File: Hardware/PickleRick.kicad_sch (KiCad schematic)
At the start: 63 parts, among them J1 RBUS, J12 Conn_01x03_Male, J14 Conn_01x07_Socket, J2 Conn_01x02_Male, J3 ST1W008S4TR2000, J4 Conn_01x03_Pin, Q1 PMV20ENR, U1 ESP32-S3, U2 DPS368, Y1 R940000171

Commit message: update
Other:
- moved on the sheet: D19
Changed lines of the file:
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@@
 	(wire
 		(pts
-			(xy 121.92 181.61) (xy 138.43 181.61)
+			(xy 121.92 182.88) (xy 133.35 182.88)
 		)
 		(stroke
@@
 	(wire
 		(pts
-			(xy 121.92 189.23) (xy 121.92 181.61)
+			(xy 121.92 190.5) (xy 121.92 182.88)
 		)
 		(stroke
@@
 	)
 	(label "JTAG_MTDI"
-		(at 168.91 184.15 0)
+		(at 163.83 185.42 0)
 		(fields_autoplaced yes)
 		(effects
@@
 	)
 	(label "JTAG_MTDO"
-		(at 138.43 186.69 180)
+		(at 133.35 187.96 180)
 		(fields_autoplaced yes)
 		(effects
@@
 	)
 	(label "JTAG_MTMS"
-		(at 138.43 184.15 180)
+		(at 133.35 185.42 180)
 		(fields_autoplaced yes)
 		(effects
@@
 		(lib_name "GND_1")
 		(lib_id "power:GND")
-		(at 121.92 189.23 0)
+		(at 121.92 190.5 0)
 		(unit 1)
 		(exclude_from_sim no)
@@
 		(fields_autoplaced yes)
 		(property "Reference" "#PWR024"
-			(at 121.92 195.58 0)
+			(at 121.92 196.85 0)
 			(effects
 				(font
@@
 		)
 		(property "Value" "GND"
-			(at 121.92 194.31 0)
+			(at 121.92 195.58 0)
 			(effects
 				(font
@@
 		)
 		(property "Footprint" ""
-			(at 121.92 189.23 0)
+			(at 121.92 190.5 0)
 			(effects
 				(font
@@
 		)
 		(property "Datasheet" ""
-			(at 121.92 189.23 0)
+			(at 121.92 190.5 0)
 			(effects
 				(font
@@
 		)
 		(property "Description" "Power symbol creates a global label with name \"GND\" , ground"
-			(at 121.92 189.23 0)
+			(at 121.92 190.5 0)
 			(effects
 				(font
@@
 	(symbol
 		(lib_id "iclr-hw:RCLAMP3346PQTNT")
-		(at 138.43 179.07 0)
+		(at 133.35 180.34 0)
 		(unit 1)
 		(exclude_from_sim no)
@@
 		(fields_autoplaced yes)
 		(property "Reference" "D19"
-			(at 153.67 171.45 0)
+			(at 148.59 172.72 0)
 			(effects
 				(font
@@
 		)
 		(property "Value" "RCLAMP3346PQTNT"
-			(at 153.67 173.99 0)
+			(at 148.59 175.26 0)
 			(effects
 				(font
@@
 		)
 		(property "Footprint" "RCLAMP3346PQTNT"
-			(at 165.1 273.99 0)
+			(at 160.02 275.26 0)
 			(effects
 				(font
@@
 		)
 		(property "Datasheet" ""
-			(at 165.1 373.99 0)
+			(at 160.02 375.26 0)
 			(effects
 				(font
@@
 		)
 		(property "Description" "ESD Suppressors / TVS Diodes 6Line ESD protection automotive grade"
-			(at 138.43 179.07 0)
+			(at 133.35 180.34 0)
 			(effects
 				(font
@@
 		)
 		(property "Height" "0.53"
-			(at 165.1 573.99 0)
+			(at 160.02 575.26 0)
 			(effects
 				(font
@@
 		)
 		(property "Mouser Part Number" "947-RCLAMP3346PQTNT"
-			(at 165.1 673.99 0)
+			(at 160.02 675.26 0)
 			(effects
 				(font
@@
 		)
 		(property "Mouser Price/Stock" "https://www.mouser.co.uk/ProductDetail/Semtech/RCLAMP3346PQTNT?qs=gTYE2QTfZfTlZML4DB76Nw%3D%3D"
-			(at 165.1 773.99 0)
+			(at 160.02 775.26 0)
 			(effects
 				(font
@@
 		)
 		(property "Manufacturer_Name" "SEMTECH"
-			(at 165.1 873.99 0)
+			(at 160.02 875.26 0)
 			(effects
 				(font
@@
 		)
 		(property "Manufacturer_Part_Number" "RCLAMP3346PQTNT"
-			(at 165.1 973.99 0)
+			(at 160.02 975.26 0)
 			(effects
 				(font

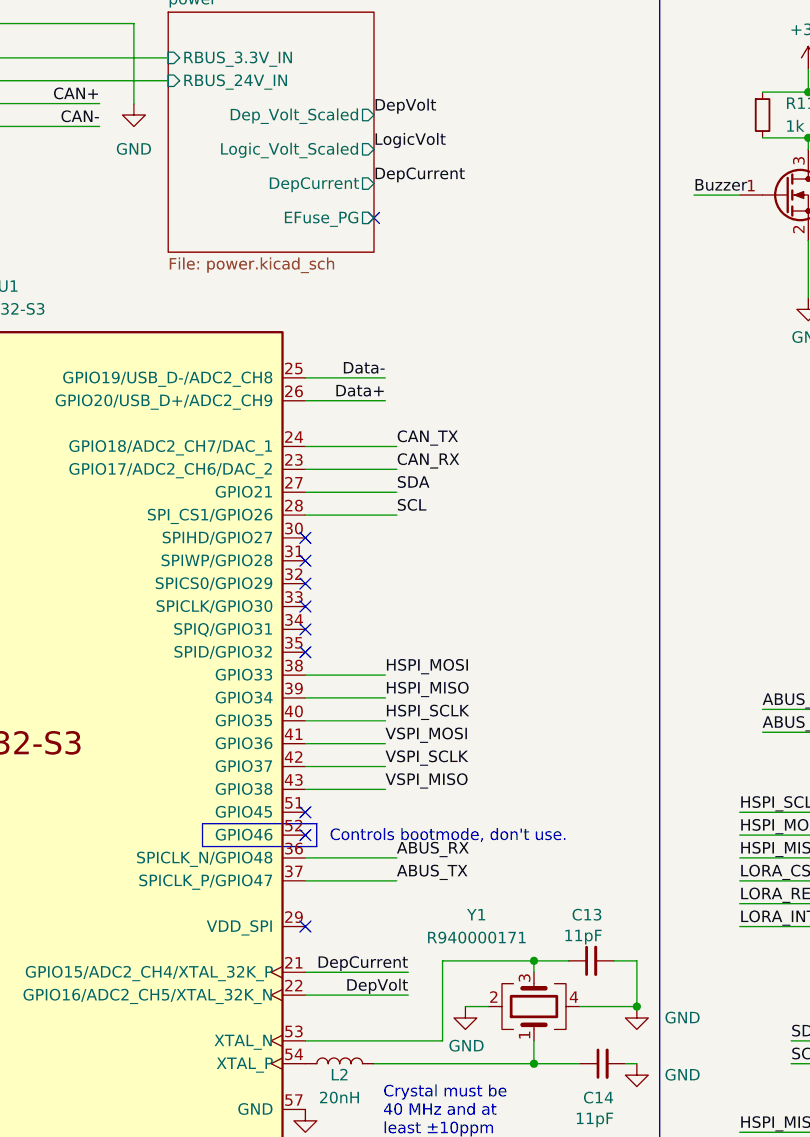
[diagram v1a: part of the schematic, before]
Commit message: replaced efuse with ina219
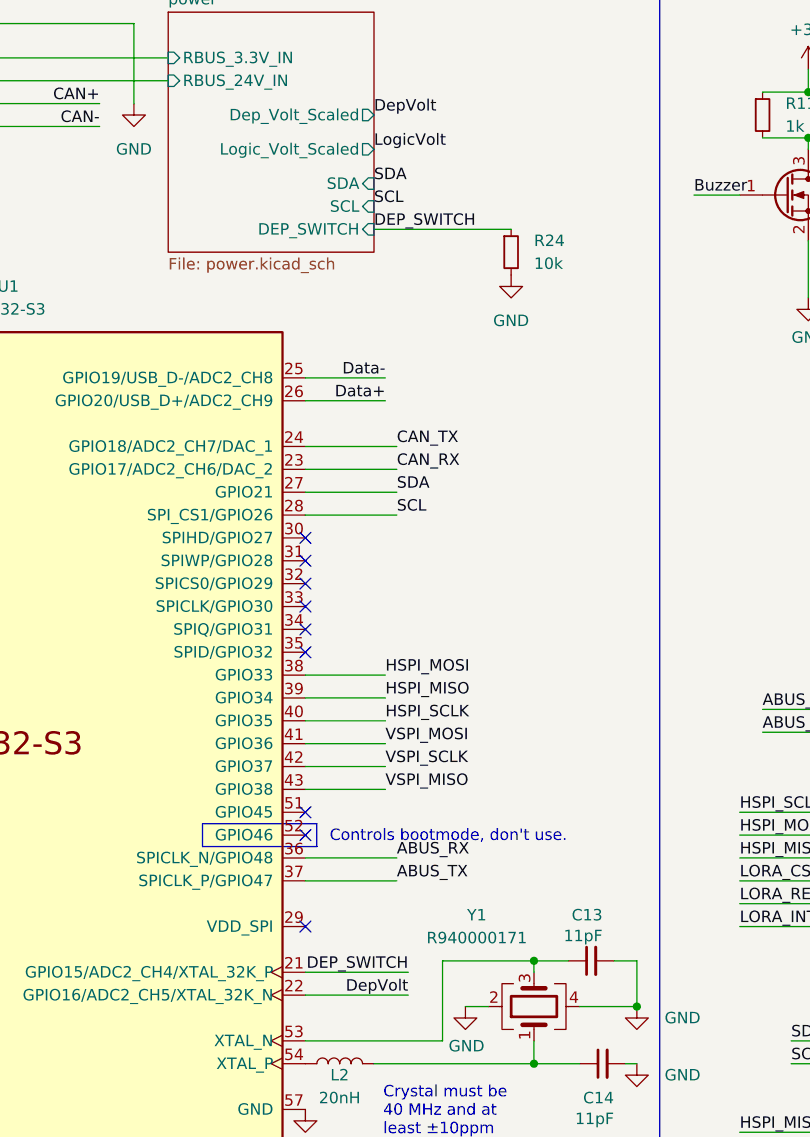
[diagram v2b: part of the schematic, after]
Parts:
- added R24: 10k, Resistor_SMD:R_0402_1005Metric, symbol Device:R_Small
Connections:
- net GND: now also R24.2
- net DepCurrent renamed DEP_SWITCH
- net DEP_SWITCH: now also R24.1
- no-connect marks 14 -> 13
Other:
- sheet power ports: added DEP_SWITCH, SCL, SDA; removed DepCurrent, EFuse_PG
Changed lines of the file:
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@@
 	)
 	(no_connect
-		(at 142.24 44.45)
-	)
-	(no_connect
 		(at 134.62 82.55)
 	)
@@
 	(wire
 		(pts
+			(xy 142.24 45.72) (xy 157.48 45.72)
+		)
+		(stroke
+			(width 0)
+			(type default)
+		)
+	)
+	(wire
+		(pts
 			(xy 226.06 123.19) (xy 234.95 123.19)
 		)
@@
 		)
 	)
+	(label "SDA"
+		(at 142.24 40.64 0)
+		(fields_autoplaced yes)
+		(effects
+			(font
+				(size 1.27 1.27)
+			)
+			(justify left bottom)
+		)
+	)
 	(label "LORA_RESET"
 		(at 60.96 92.71 180)
@@
 		)
 	)
-	(label "JTAG_MTMS"
-		(at 39.37 125.73 0)
+	(label "DEP_SWITCH"
+		(at 142.24 45.72 0)
 		(fields_autoplaced yes)
 		(effects
@@
 		)
 	)
-	(label "CAN-"
-		(at 114.3 187.96 0)
+	(label "JTAG_MTMS"
+		(at 39.37 125.73 0)
 		(fields_autoplaced yes)
 		(effects
@@
 		)
 	)
-	(label "DepCurrent"
-		(at 142.24 40.64 0)
+	(label "CAN-"
+		(at 114.3 187.96 0)
 		(fields_autoplaced yes)
 		(effects
@@
 		)
 	)
+	(label "SCL"
+		(at 142.24 43.18 0)
+		(fields_autoplaced yes)
+		(effects
+			(font
+				(size 1.27 1.27)
+			)
+			(justify left bottom)
+		)
+	)
 	(label "IMU2_CS"
 		(at 60.96 97.79 180)
@@
 		)
 	)
-	(label "DepCurrent"
+	(label "DEP_SWITCH"
 		(at 146.05 128.27 180)
 		(fields_autoplaced yes)
@@
 	)
 	(symbol
+		(lib_name "GND_2")
+		(lib_id "power:GND")
+		(at 157.48 50.8 0)
+		(unit 1)
+		(exclude_from_sim no)
+		(in_bom yes)
+		(on_board yes)
+		(dnp no)
+		(fields_autoplaced yes)
+		(property "Reference" "#PWR098"
+			(at 157.48 57.15 0)
+			(effects
+				(font
+					(size 1.27 1.27)
+				)
+				(hide yes)
+			)
+		)
+		(property "Value" "GND"
+			(at 157.48 55.88 0)
+			(effects
+				(font
+					(size 1.27 1.27)
+				)
+			)
+		)
+		(property "Footprint" ""
+			(at 157.48 50.8 0)
+			(effects
+				(font
+					(size 1.27 1.27)
+				)
+				(hide yes)
+			)
+		)
+		(property "Datasheet" ""
+			(at 157.48 50.8 0)
+			(effects
+				(font
+					(size 1.27 1.27)
+				)
+				(hide yes)
+			)
+		)
+		(property "Description" "Power symbol creates a global label with name \"GND\" , ground"
+			(at 157.48 50.8 0)
+			(effects
+				(font
+					(size 1.27 1.27)
+				)
+				(hide yes)
+			)
+		)
+		(pin "1"
+		)
+		(instances
+			(project ""
+				(path "/e63e39d7-6ac0-4ffd-8aa3-1841a4541b55"
+					(reference "#PWR098")
+					(unit 1)
+				)
+			)
+		)
+	)
+	(symbol
 		(lib_id "Device:LED_Small")
 		(at 27.94 64.135 0)
@@
 	(symbol
 		(lib_id "Device:R_Small")
+		(at 157.48 48.26 0)
+		(unit 1)
+		(exclude_from_sim no)
+		(in_bom yes)
+		(on_board yes)
+		(dnp no)
+		(fields_autoplaced yes)
+		(property "Reference" "R24"
+			(at 160.02 46.9899 0)
+			(effects
+				(font
+					(size 1.27 1.27)
+				)
+				(justify left)
+			)
+		)
+		(property "Value" "10k"
+			(at 160.02 49.5299 0)
+			(effects
+				(font
+					(size 1.27 1.27)
+				)
+				(justify left)
+			)
+		)
+		(property "Footprint" "Resistor_SMD:R_0402_1005Metric"
+			(at 157.48 48.26 0)
+			(effects
+				(font
+					(size 1.27 1.27)
+				)
+				(hide yes)
+			)
+		)
+		(property "Datasheet" "~"
+			(at 157.48 48.26 0)
+			(effects
+				(font
+					(size 1.27 1.27)
+				)
+				(hide yes)
+			)
+		)
+		(property "Description" "Resistor, small symbol"
+			(at 157.48 48.26 0)
+			(effects
+				(font
+					(size 1.27 1.27)
+				)
+				(hide yes)
+			)
+		)
+		(pin "2"
+		)
+		(pin "1"
+		)
+		(instances
+			(project ""
+				(path "/e63e39d7-6ac0-4ffd-8aa3-1841a4541b55"
+					(reference "R24")
+					(unit 1)
+				)
+			)
+		)
+	)
+	(symbol
+		(lib_id "Device:R_Small")
 		(at 35.56 29.21 270)
 		(unit 1)
@@
 			)
 		)
-		(pin "DepCurrent" output
+		(pin "SDA" input
 			(at 142.24 40.64 0)
 			(effects
@@
 			)
 		)
-		(pin "EFuse_PG" output
-			(at 142.24 44.45 0)
+		(pin "SCL" input
+			(at 142.24 43.18 0)
+			(effects
+				(font
+					(size 1.27 1.27)
+				)
+				(justify right)
+			)
+		)
+		(pin "DEP_SWITCH" input
+			(at 142.24 45.72 0)
 			(effects
 				(font

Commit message: fixes
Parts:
- D19: footprint RCLAMP3346PQTNT -> iclr-hw:RCLAMP3346PQTNT
- R34, R35: value 4.7k -> 2.2k
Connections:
- no-connect marks 13 -> 16
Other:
- sheet USB -> UART ports: added none; removed 3.3V
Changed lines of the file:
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@@
 	)
 	(no_connect
+		(at 133.35 180.34)
+	)
+	(no_connect
 		(at 240.03 69.85)
 	)
 	(no_connect
+		(at 163.83 180.34)
+	)
+	(no_connect
 		(at 134.62 90.17)
 	)
@@
 	)
 	(no_connect
+		(at 163.83 182.88)
+	)
+	(no_connect
 		(at 134.62 123.19)
 	)
@@
 	(wire
 		(pts
-			(xy 97.79 156.21) (xy 101.6 156.21)
-		)
-		(stroke
-			(width 0)
-			(type default)
-		)
-	)
-	(wire
-		(pts
 			(xy 243.84 27.94) (xy 259.08 27.94)
 		)
@@
 			)
 		)
-		(property "Value" "4.7k"
+		(property "Value" "2.2k"
 			(at 257.81 144.7799 0)
 			(effects
@@
 	(symbol
 		(lib_id "power:+3.3V")
-		(at 101.6 156.21 0)
-		(unit 1)
-		(exclude_from_sim no)
-		(in_bom yes)
-		(on_board yes)
-		(dnp no)
-		(property "Reference" "#PWR016"
-			(at 101.6 160.02 0)
-			(effects
-				(font
-					(size 1.27 1.27)
-				)
-				(hide yes)
-			)
-		)
-		(property "Value" "+3V3"
-			(at 101.981 151.8158 0)
-			(effects
-				(font
-					(size 1.27 1.27)
-				)
-			)
-		)
-		(property "Footprint" ""
-			(at 101.6 156.21 0)
-			(effects
-				(font
-					(size 1.27 1.27)
-				)
-				(hide yes)
-			)
-		)
-		(property "Datasheet" ""
-			(at 101.6 156.21 0)
-			(effects
-				(font
-					(size 1.27 1.27)
-				)
-				(hide yes)
-			)
-		)
-		(property "Description" ""
-			(at 101.6 156.21 0)
-			(effects
-				(font
-					(size 1.27 1.27)
-				)
-				(hide yes)
-			)
-		)
-		(pin "1"
-		)
-		(instances
-			(project "PickleRick"
-				(path "/e63e39d7-6ac0-4ffd-8aa3-1841a4541b55"
-					(reference "#PWR016")
-					(unit 1)
-				)
-			)
-		)
-	)
-	(symbol
-		(lib_id "power:+3.3V")
 		(at 251.46 44.45 0)
 		(unit 1)
@@
 			)
 		)
-		(property "Value" "4.7k"
+		(property "Value" "2.2k"
 			(at 262.89 144.7799 0)
 			(effects
@@
 			)
 		)
-		(property "Footprint" "RCLAMP3346PQTNT"
+		(property "Footprint" "iclr-hw:RCLAMP3346PQTNT"
 			(at 160.02 275.26 0)
 			(effects
@@
 			)
 		)
-		(pin "3.3V" output
-			(at 97.79 156.21 0)
-			(effects
-				(font
-					(size 1.27 1.27)
-				)
-				(justify right)
-			)
-		)

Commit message: Adding some 3d models
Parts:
- LS1: footprint iclr-hw:CMT052575SMTTR -> iclr:CMT052575SMTTR
- Y1: footprint Crystal:Crystal_SMD_2016-4Pin_2.0x1.6mm -> iclr:Crystal_SMD_2016-4Pin_2.0x1.6mm

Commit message: Full v3 Pickle 3d model
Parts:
- J14: footprint Connector_Molex:Molex_Pico-Clasp_202396-0707_1x07-1MP_P1.00mm_Horizontal -> iclr:Molex_Pico-Clasp_202396-0707_1x07-1MP_P1.00mm_Horizontal
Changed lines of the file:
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@@
 			)
 		)
-		(property "Footprint" "Connector_Molex:Molex_Pico-Clasp_202396-0707_1x07-1MP_P1.00mm_Horizontal"
+		(property "Footprint" "iclr:Molex_Pico-Clasp_202396-0707_1x07-1MP_P1.00mm_Horizontal"
 			(at 264.16 33.02 0)
 			(effects

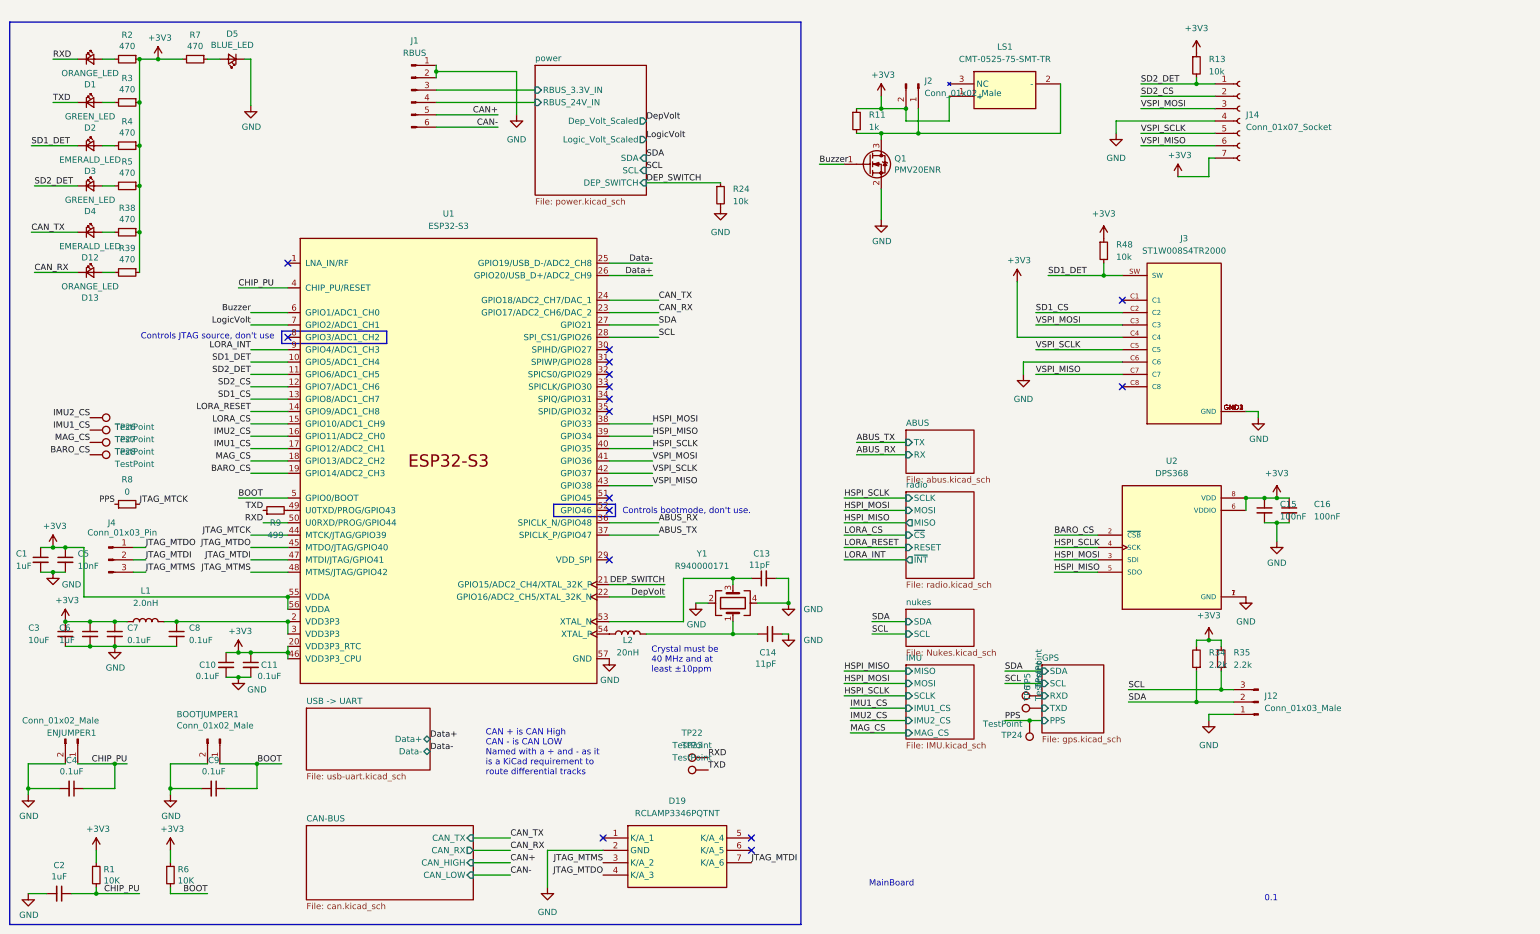
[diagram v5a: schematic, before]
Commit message: Restore controlled IMU interface in schematic hierarchy
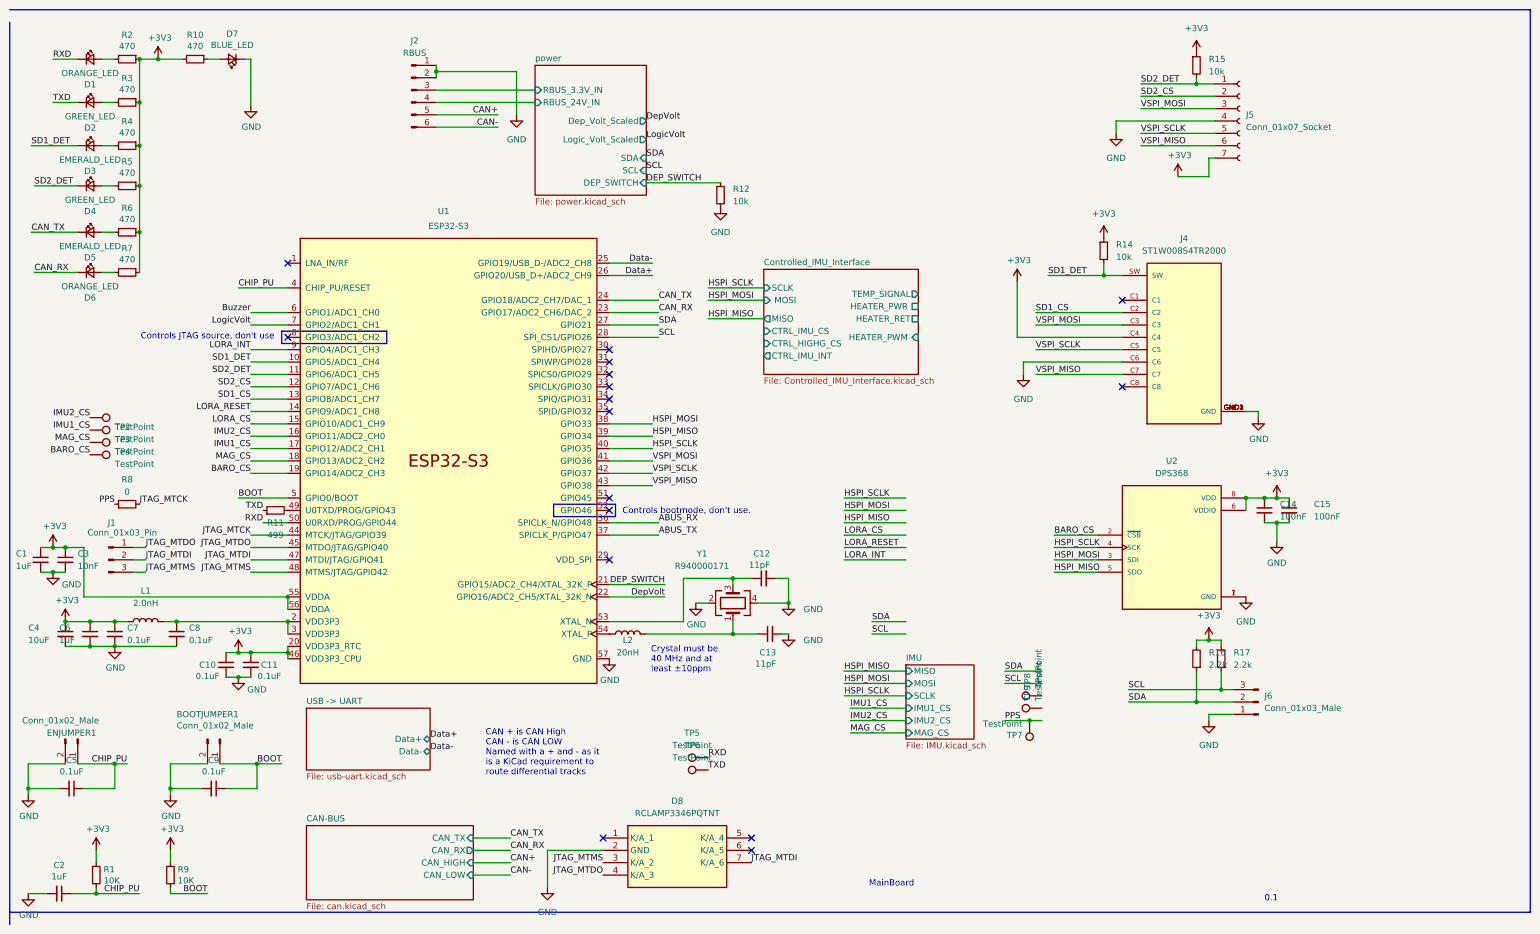
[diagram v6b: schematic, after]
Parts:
- removed J2: Conn_01x02_Male, Connector_JST:JST_PH_B2B-PH-K_1x02_P2.00mm_Vertical, symbol Connector:Conn_01x02_Male
- removed LS1: CMT-0525-75-SMT-TR, iclr:CMT052575SMTTR, symbol iclr-hw:CMT-0525-75-SMT-TR
- removed Q1: PMV20ENR, Package_TO_SOT_SMD:SOT-23, symbol Device:Q_NMOS_GSD
- removed R11: 1k, Resistor_SMD:R_0402_1005Metric, symbol Device:R_Small
- renumbered C13 to C12, C14 to C13, C15 to C14, C16 to C15, C5 to C3, C3 to C4, C4 to C5, D12 to D5, D13 to D6, D5 to D7, D19 to D8, J4 to J1, J1 to J2, J3 to J4, J14 to J5, J12 to J6, R7 to R10, R9 to R11, R24 to R12, R48 to R14, R13 to R15, R34 to R16, R35 to R17, R38 to R6, R39 to R7, R6 to R9, TP25 to TP1, TP26 to TP2, TP27 to TP3, TP28 to TP4, TP22 to TP5, TP23 to TP6, TP24 to TP7, TP5 to TP8, TP6 to TP9
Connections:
- net GPS/RXD: no longer names the net of TP8.1
- net GPS/TXD: no longer names the net of TP9.1
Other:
- removed sheet ABUS
- removed sheet GPS
- removed sheet nukes
- removed sheet radio
- added sheet Controlled_IMU_Interface (Controlled_IMU_Interface.kicad_sch)
